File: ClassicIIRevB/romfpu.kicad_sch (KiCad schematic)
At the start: 1 part, among them J10 ROM/FPU EXPANSION SLOT

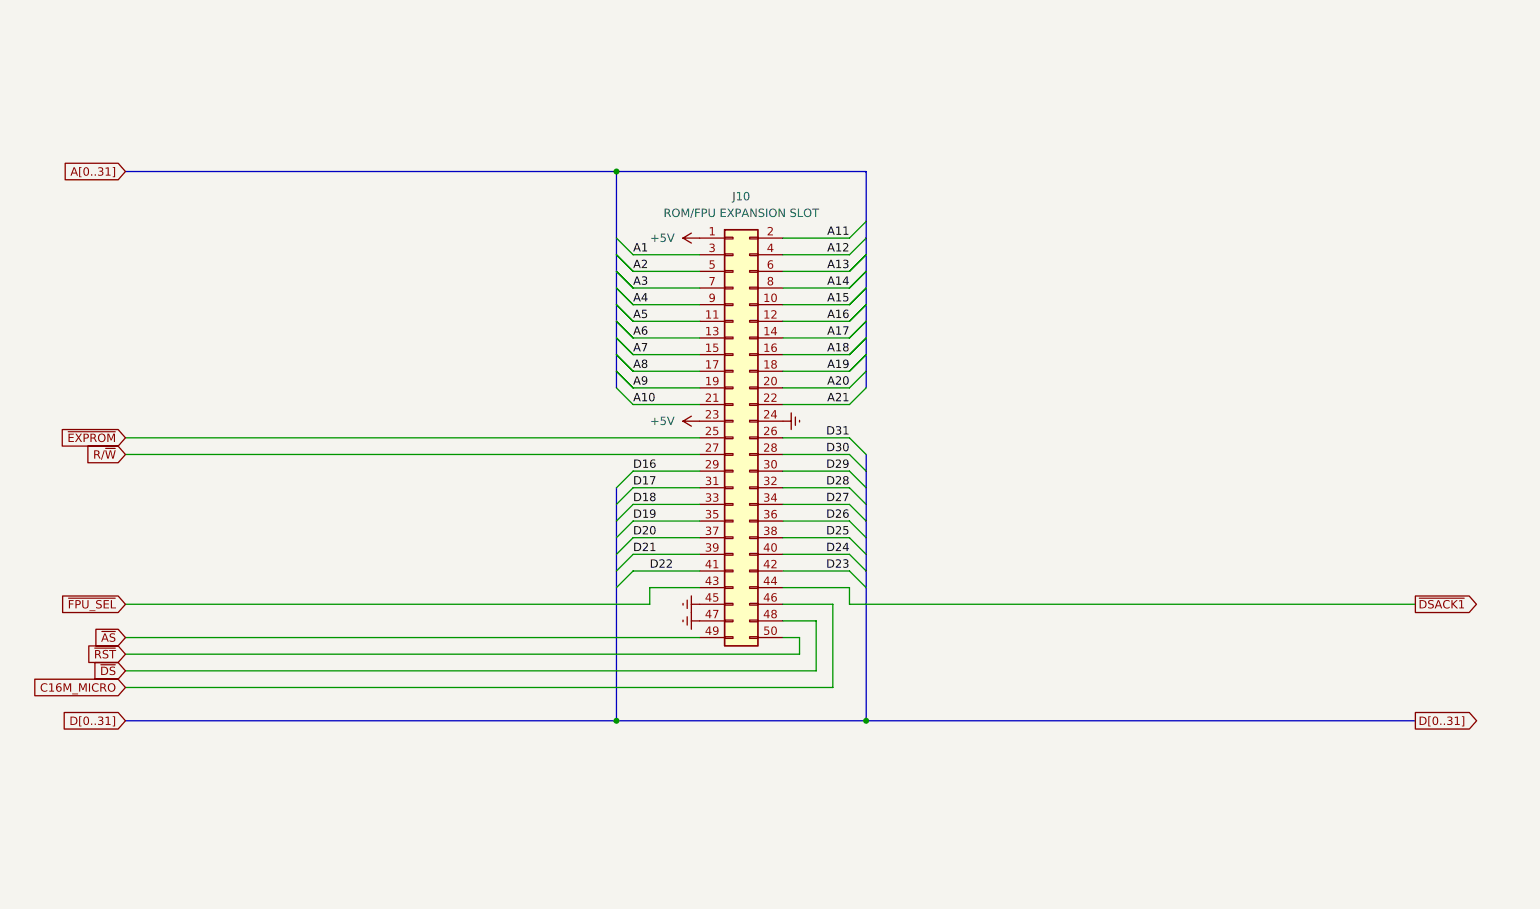
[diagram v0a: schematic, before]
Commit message: Show smaller ROM footprints
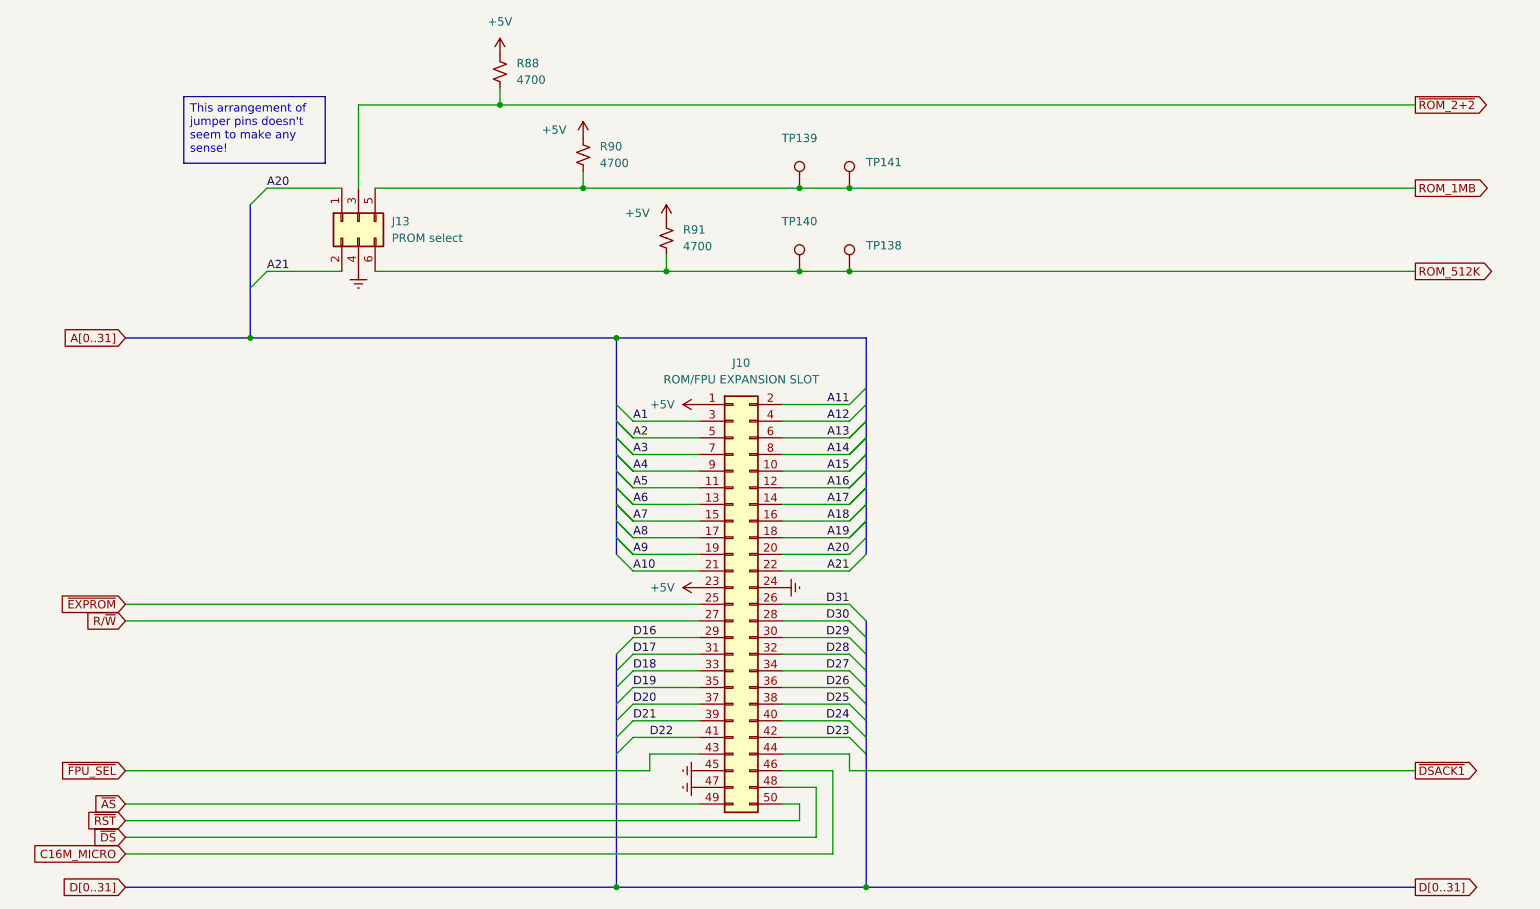
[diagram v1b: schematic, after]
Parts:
- added J13: PROM select, Connector_PinHeader_2.54mm:PinHeader_2x03_P2.54mm_Vertical, symbol Connector_Generic:Conn_02x03_Odd_Even
- added R88, R90, R91: 4700, MyPackage:SMD_0805_2012Metric_Pad1.25x1.65mm, symbol Device:R_Small_US
- added TP138, TP139, TP140, TP141: ~, MyPackage:TestPoint_THTPad_D1.0mm_Drill0.5mm, symbol Connector:TestPoint
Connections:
- net +5V: now also R88.2, R90.2, R91.2
- net A20: now also J13.1 (Pin_1)
- net A21: now also J13.2 (Pin_2)
- net GND: now also J13.4 (Pin_4)
- new net ROM_1MB: J13.5 (Pin_5), R90.1, TP139.1, TP141.1
- new net ROM_512K: J13.6 (Pin_6), R91.1, TP138.1, TP140.1
- new net ~{ROM_2+2}: J13.3 (Pin_3), R88.1
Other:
- moved on the sheet: J10

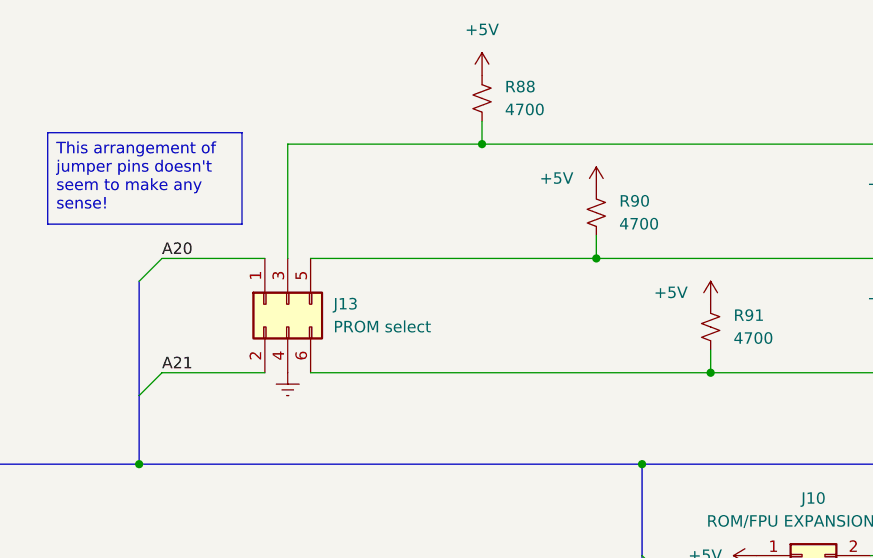
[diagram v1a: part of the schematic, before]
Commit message: improved footprints and silkscreens
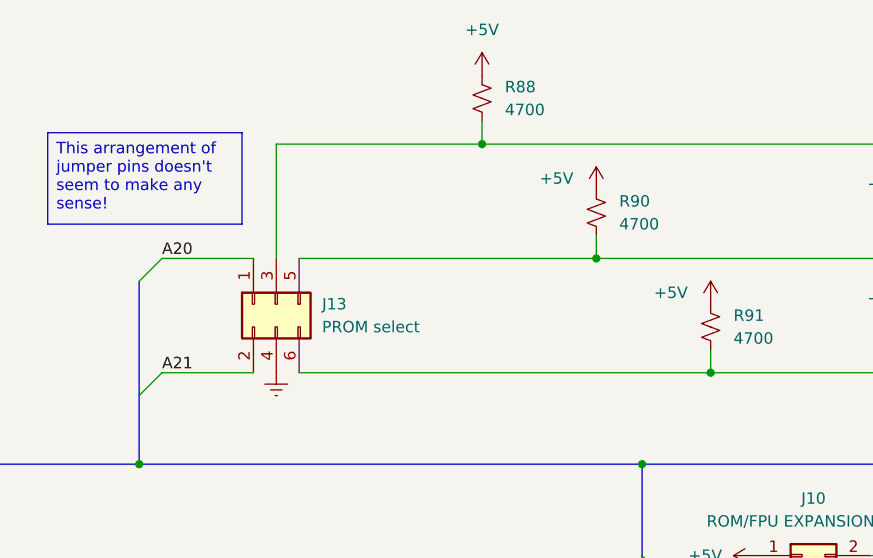
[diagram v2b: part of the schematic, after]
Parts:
- J10: footprint MyPackage:MacClassicROMFPU_2x25_P2.54mm_Vertical -> Connector_Imports:TE_5-102567-6
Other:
- moved on the sheet: J13
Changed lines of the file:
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@@
 	(title_block
 		(title "Macintosh Classic II Revision B")
-		(date "2025-05-31")
+		(date "2025-06-04")
 		(company "Apple Computer")
 		(comment 1 "drawn by Bradley Bell")
@@
 	(wire
 		(pts
-			(xy 80.01 40.64) (xy 101.6 40.64)
+			(xy 78.74 40.64) (xy 101.6 40.64)
 		)
 		(stroke
@@
 	(wire
 		(pts
-			(xy 66.04 66.04) (xy 77.47 66.04)
+			(xy 66.04 66.04) (xy 76.2 66.04)
 		)
 		(stroke
@@
 	(wire
 		(pts
-			(xy 127 66.04) (xy 82.55 66.04)
+			(xy 127 66.04) (xy 81.28 66.04)
 		)
 		(stroke
@@
 	(wire
 		(pts
-			(xy 80.01 40.64) (xy 80.01 53.34)
+			(xy 78.74 40.64) (xy 78.74 53.34)
 		)
 		(stroke
@@
 	(wire
 		(pts
-			(xy 82.55 53.34) (xy 114.3 53.34)
+			(xy 81.28 53.34) (xy 114.3 53.34)
 		)
 		(stroke
@@
 	(wire
 		(pts
-			(xy 77.47 53.34) (xy 66.04 53.34)
+			(xy 76.2 53.34) (xy 66.04 53.34)
 		)
 		(stroke
@@
 			)
 		)
-		(property "Footprint" "MyPackage:MacClassicROMFPU_2x25_P2.54mm_Vertical"
+		(property "Footprint" "Connector_Imports:TE_5-102567-6"
 			(at 137.16 116.84 0)
 			(effects
@@
 	(symbol
 		(lib_id "Connector_Generic:Conn_02x03_Odd_Even")
-		(at 80.01 58.42 90)
+		(at 78.74 58.42 90)
 		(mirror x)
 		(unit 1)
@@
 		(fields_autoplaced yes)
 		(property "Reference" "J13"
-			(at 85.09 58.4199 90)
+			(at 83.82 58.4199 90)
 			(effects
 				(font
@@
 		)
 		(property "Value" "PROM select"
-			(at 85.09 60.9599 90)
+			(at 83.82 60.9599 90)
 			(effects
 				(font
@@
 		)
 		(property "Footprint" "Connector_PinHeader_2.54mm:PinHeader_2x03_P2.54mm_Vertical"
-			(at 80.01 58.42 0)
+			(at 78.74 58.42 0)
 			(effects
 				(font
@@
 		)
 		(property "Datasheet" "~"
-			(at 80.01 58.42 0)
+			(at 78.74 58.42 0)
 			(effects
 				(font
@@
 		)
 		(property "Description" "Generic connector, double row, 02x03, odd/even pin numbering scheme (row 1 odd numbers, row 2 even numbers), script generated (kicad-library-utils/schlib/autogen/connector/)"
-			(at 80.01 58.42 0)
+			(at 78.74 58.42 0)
 			(effects
 				(font
@@
 	(symbol
 		(lib_id "power:GNDREF")
-		(at 80.01 66.04 0)
+		(at 78.74 66.04 0)
 		(unit 1)
 		(exclude_from_sim no)
@@
 		(fields_autoplaced yes)
 		(property "Reference" "#PWR0199"
-			(at 80.01 72.39 0)
+			(at 78.74 72.39 0)
 			(effects
 				(font
@@
 		)
 		(property "Value" "GND"
-			(at 80.0101 69.85 90)
+			(at 78.7401 69.85 90)
 			(effects
 				(font
@@
 		)
 		(property "Footprint" ""
-			(at 80.01 66.04 0)
+			(at 78.74 66.04 0)
 			(effects
 				(font
@@
 		)
 		(property "Datasheet" ""
-			(at 80.01 66.04 0)
+			(at 78.74 66.04 0)
 			(effects
 				(font
@@
 		)
 		(property "Description" "Power symbol creates a global label with name \"GNDREF\" , reference supply ground"
-			(at 80.01 66.04 0)
-			(effects
-				(font
+			(at 78.74 66.04 0)
+			(effects
+				(font

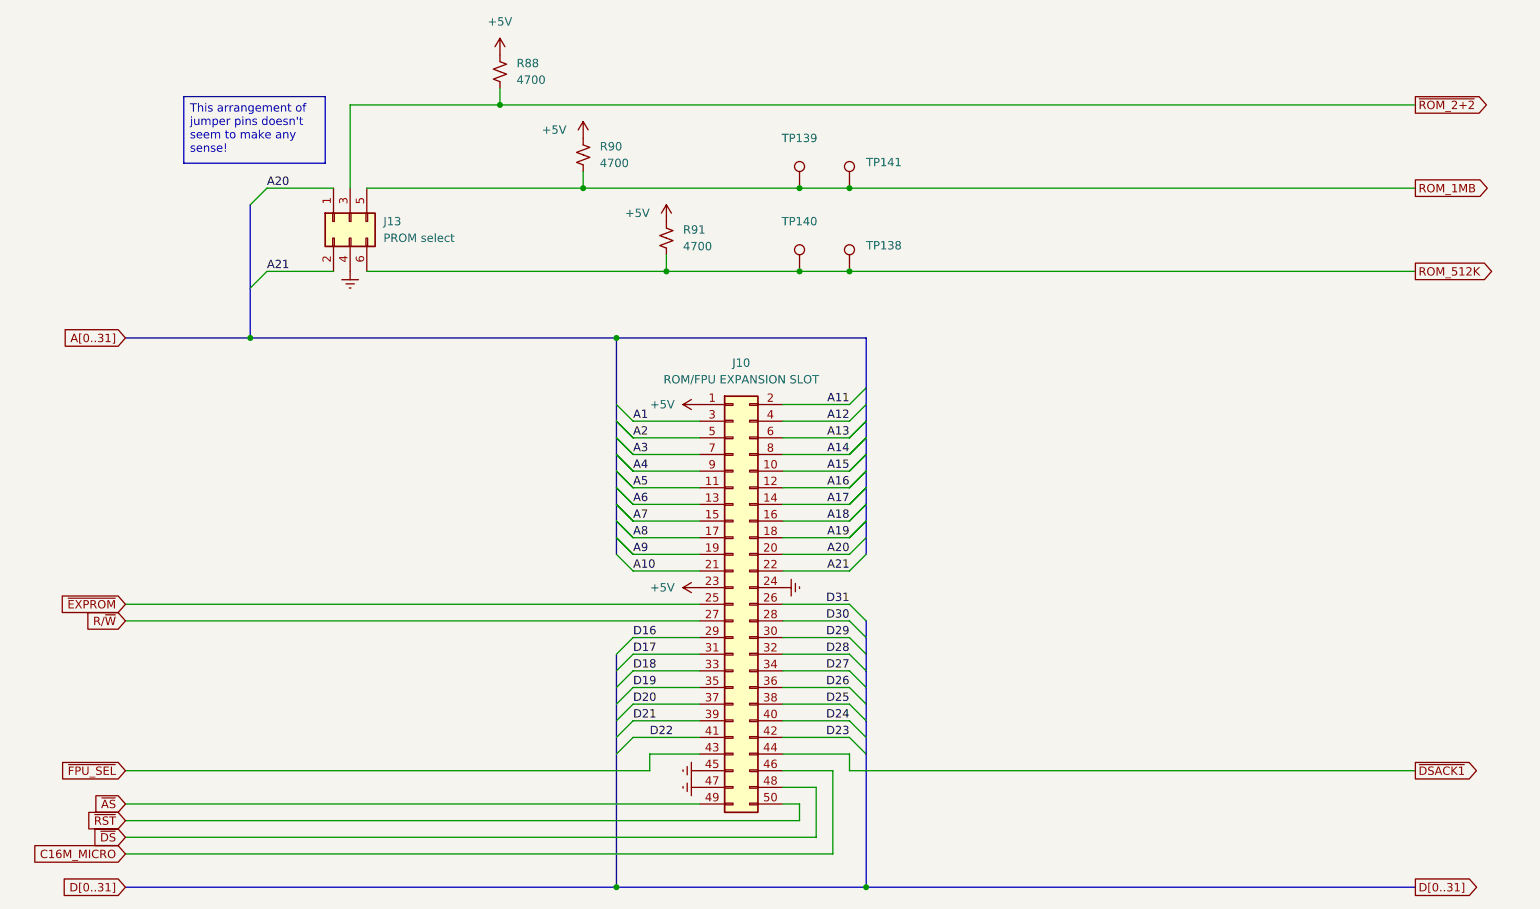
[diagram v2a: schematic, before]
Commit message: Switch to some "official" net names
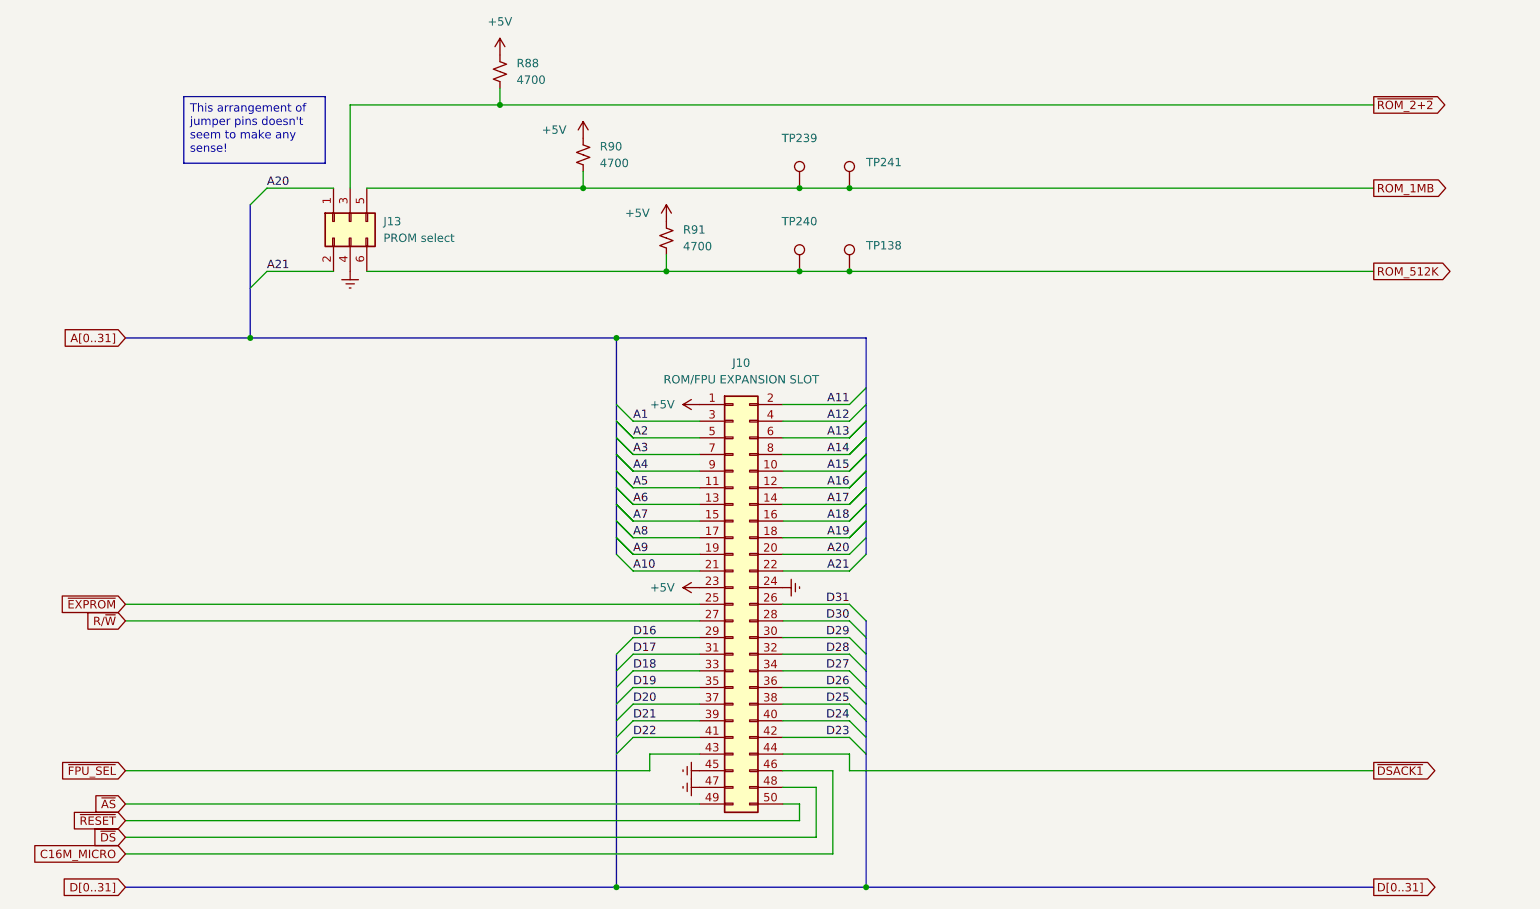
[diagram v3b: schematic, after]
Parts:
- renumbered TP139 to TP239, TP140 to TP240, TP141 to TP241
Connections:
- net ~{RST} renamed ~{RESET}
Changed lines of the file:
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@@
 	(wire
 		(pts
-			(xy 154.94 66.04) (xy 241.3 66.04)
+			(xy 154.94 66.04) (xy 234.95 66.04)
 		)
 		(stroke
@@
 	(wire
 		(pts
-			(xy 154.94 142.24) (xy 241.3 142.24)
+			(xy 154.94 142.24) (xy 234.95 142.24)
 		)
 		(stroke
@@
 	(bus
 		(pts
-			(xy 157.48 160.02) (xy 241.3 160.02)
+			(xy 157.48 160.02) (xy 234.95 160.02)
 		)
 		(stroke
@@
 	(wire
 		(pts
-			(xy 154.94 53.34) (xy 241.3 53.34)
+			(xy 154.94 53.34) (xy 234.95 53.34)
 		)
 		(stroke
@@
 	(wire
 		(pts
-			(xy 101.6 40.64) (xy 241.3 40.64)
+			(xy 101.6 40.64) (xy 234.95 40.64)
 		)
 		(stroke
@@
 	)
 	(label "D22"
-		(at 124.46 137.16 0)
+		(at 121.92 137.16 0)
 		(effects
 			(font
@@
 	(global_label "D[0..31]"
 		(shape output)
-		(at 241.3 160.02 0)
+		(at 234.95 160.02 0)
 		(fields_autoplaced yes)
 		(effects
@@
 		)
 		(property "Intersheetrefs" "${INTERSHEET_REFS}"
-			(at 252.0867 160.02 0)
+			(at 245.7367 160.02 0)
 			(effects
 				(font
@@
 	(global_label "ROM_512K"
 		(shape output)
-		(at 241.3 66.04 0)
+		(at 234.95 66.04 0)
 		(fields_autoplaced yes)
 		(effects
@@
 		)
 		(property "Intersheetrefs" "${INTERSHEET_REFS}"
-			(at 252.8123 66.04 0)
+			(at 246.4623 66.04 0)
 			(effects
 				(font
@@
 		)
 	)
-	(global_label "~{RST}"
+	(global_label "~{RESET}"
 		(shape input)
 		(at 44.45 149.86 180)
@@
 		)
 		(property "Intersheetrefs" "${INTERSHEET_REFS}"
-			(at 38.0177 149.86 0)
+			(at 35.7197 149.86 0)
 			(effects
 				(font
@@
 	(global_label "~{DSACK1}"
 		(shape output)
-		(at 241.3 142.24 0)
+		(at 234.95 142.24 0)
 		(fields_autoplaced yes)
 		(effects
@@
 		)
 		(property "Intersheetrefs" "${INTERSHEET_REFS}"
-			(at 251.6028 142.24 0)
+			(at 245.2528 142.24 0)
 			(effects
 				(font
@@
 	(global_label "ROM_1MB"
 		(shape output)
-		(at 241.3 53.34 0)
+		(at 234.95 53.34 0)
 		(fields_autoplaced yes)
 		(effects
@@
 		)
 		(property "Intersheetrefs" "${INTERSHEET_REFS}"
-			(at 252.8123 53.34 0)
+			(at 246.4623 53.34 0)
 			(effects
 				(font
@@
 	(global_label "~{ROM_2+2}"
 		(shape output)
-		(at 241.3 40.64 0)
+		(at 234.95 40.64 0)
 		(fields_autoplaced yes)
 		(effects
@@
 		)
 		(property "Intersheetrefs" "${INTERSHEET_REFS}"
-			(at 252.9333 40.64 0)
+			(at 246.5833 40.64 0)
 			(effects
 				(font
@@
 		(dnp no)
 		(fields_autoplaced yes)
-		(property "Reference" "TP140"
+		(property "Reference" "TP240"
 			(at 147.32 58.42 0)
 			(effects
@@
 			(project "ClassicIIRevB"
 				(path "/08c23af6-72f1-4a8f-a60c-b986fe71300f/bc80051c-6830-456e-b0c4-e1f5b90e7af5"
-					(reference "TP140")
+					(reference "TP240")
 					(unit 1)
 				)
@@
 		(dnp no)
 		(fields_autoplaced yes)
-		(property "Reference" "TP139"
+		(property "Reference" "TP239"
 			(at 147.32 45.72 0)
 			(effects
@@
 			(project "ClassicIIRevB"
 				(path "/08c23af6-72f1-4a8f-a60c-b986fe71300f/bc80051c-6830-456e-b0c4-e1f5b90e7af5"
-					(reference "TP139")
+					(reference "TP239")
 					(unit 1)
 				)
@@
 		(dnp no)
 		(fields_autoplaced yes)
-		(property "Reference" "TP141"
+		(property "Reference" "TP241"
 			(at 157.48 49.4029 0)
 			(effects
@@
 			(project "ClassicIIRevB"
 				(path "/08c23af6-72f1-4a8f-a60c-b986fe71300f/bc80051c-6830-456e-b0c4-e1f5b90e7af5"
-					(reference "TP141")
+					(reference "TP241")
 					(unit 1)
 				)

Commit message: update exports
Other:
- title: Macintosh Classic II Revision B -> Macintosh Classic II (Later Revision)
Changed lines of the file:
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@@
 	(paper "USLetter")
 	(title_block
-		(title "Macintosh Classic II Revision B")
-		(date "2025-06-04")
+		(title "Macintosh Classic II (Later Revision)")
+		(date "2025-06-16")
 		(company "Apple Computer")
 		(comment 1 "drawn by Bradley Bell")
